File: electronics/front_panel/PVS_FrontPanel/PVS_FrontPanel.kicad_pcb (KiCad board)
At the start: 2 copper layers, 60.4 x 100.4 mm, 3 parts

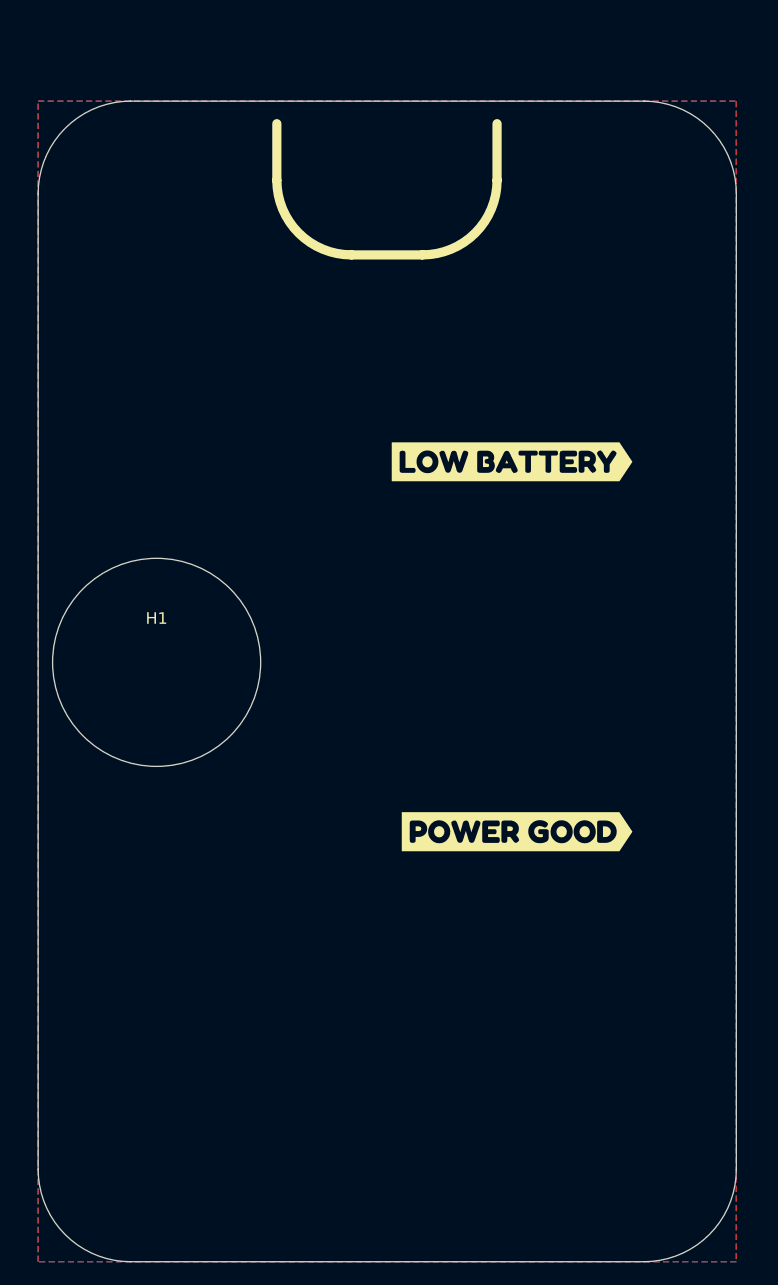
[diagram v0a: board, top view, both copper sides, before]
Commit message: Front panel improvement
Began working on the front panel design
Added to mech assembly
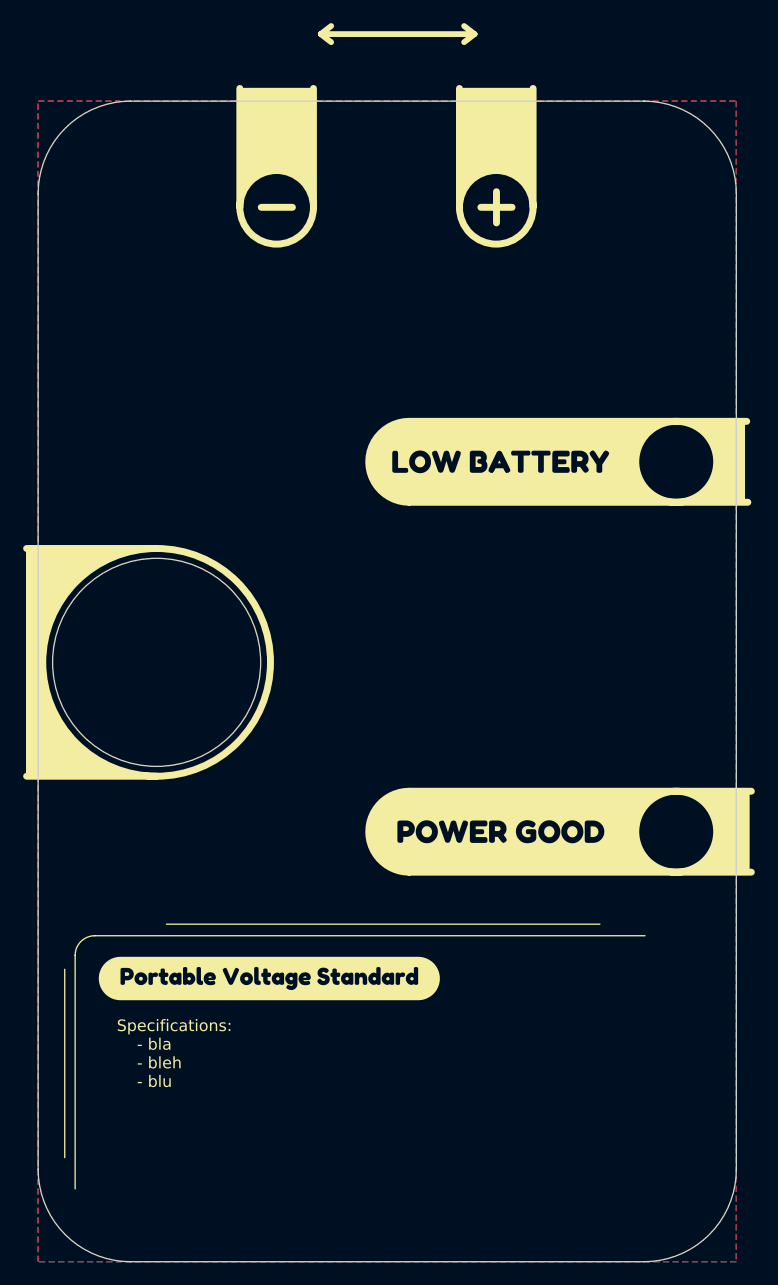
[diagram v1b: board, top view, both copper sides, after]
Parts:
- removed kibuzzard-678FE920: G***, kibuzzard-678FE920
- removed kibuzzard-678FE930: G***, kibuzzard-678FE930
- added kibuzzard-67929152: G***, kibuzzard-67929152, F.Cu at (158.2, 78.4)
- added kibuzzard-6792930C: G***, kibuzzard-6792930C, F.Cu at (158.2, 110.4)
- added kibuzzard-67929C6A: G***, kibuzzard-67929C6A, F.Cu at (138.4, 123.1)
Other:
- board text added: "Specifications: - bla - bleh - blu"
